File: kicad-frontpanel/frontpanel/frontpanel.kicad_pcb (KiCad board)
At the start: 2 copper layers, 45.7 x 128.5 mm, 0 parts

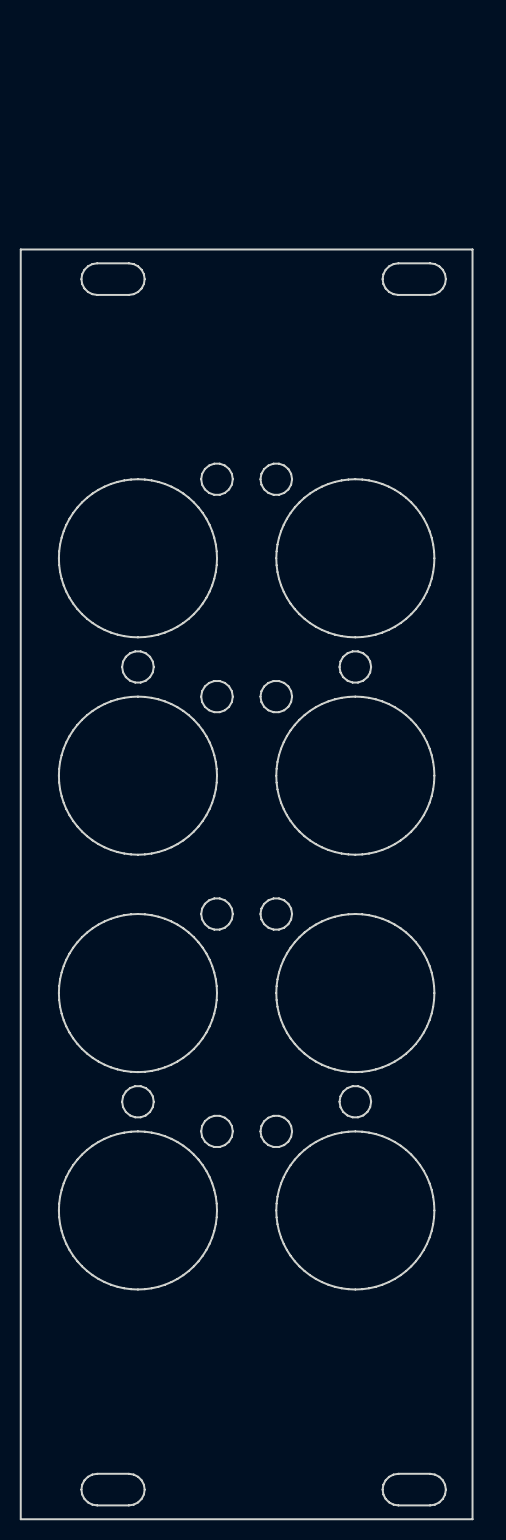
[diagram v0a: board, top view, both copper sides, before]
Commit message: Updates to frontpanels, schematics and pcbs.
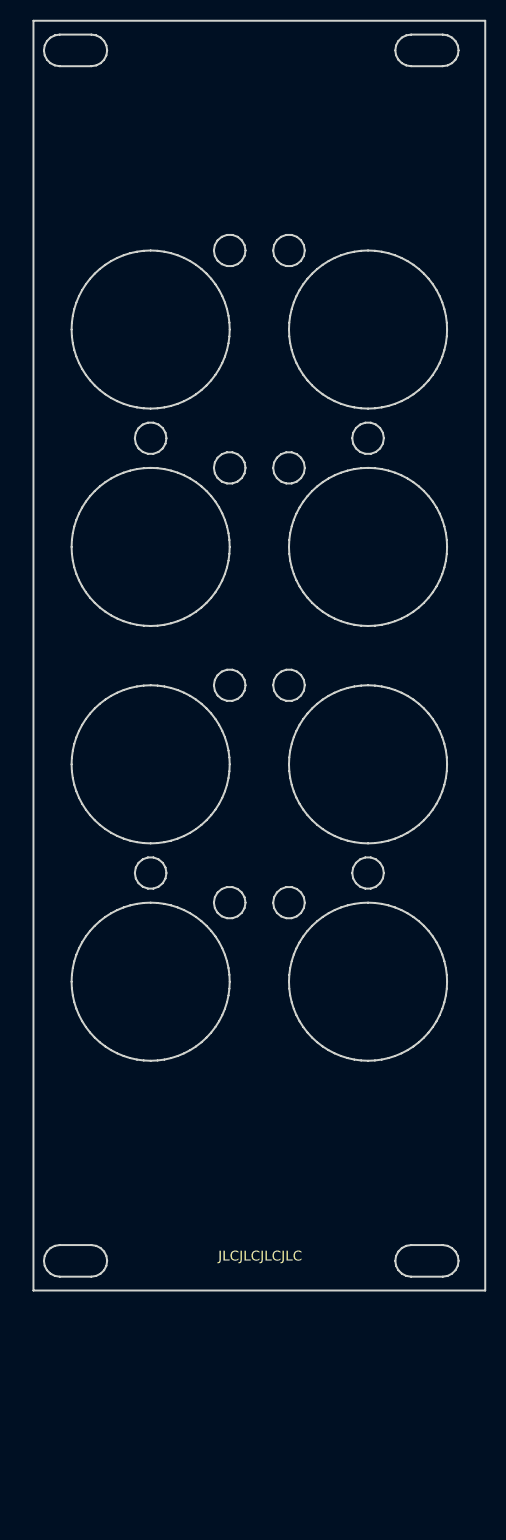
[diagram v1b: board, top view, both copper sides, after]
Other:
- outline, holes or cut-outs redrawn
- board text added: "IN"
- board text added: "JLCJLCJLCJLC"
- board text added: "MIDI ROUTER"
- board text added: "MIDI x4"
- board text added: "OUT"
- board text added: "TOMARUS"
- board text removed: "MIDI X4"
- board text removed: "TOMARUS MIDIROUTER"
